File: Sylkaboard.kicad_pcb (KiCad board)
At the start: 2 copper layers, 149.6 x 125.6 mm, 117 parts, among them J1 Conn_01x04_Pin, J2 USB_C_Receptacle_USB2.0_16P, U1 RP2040-ZERO

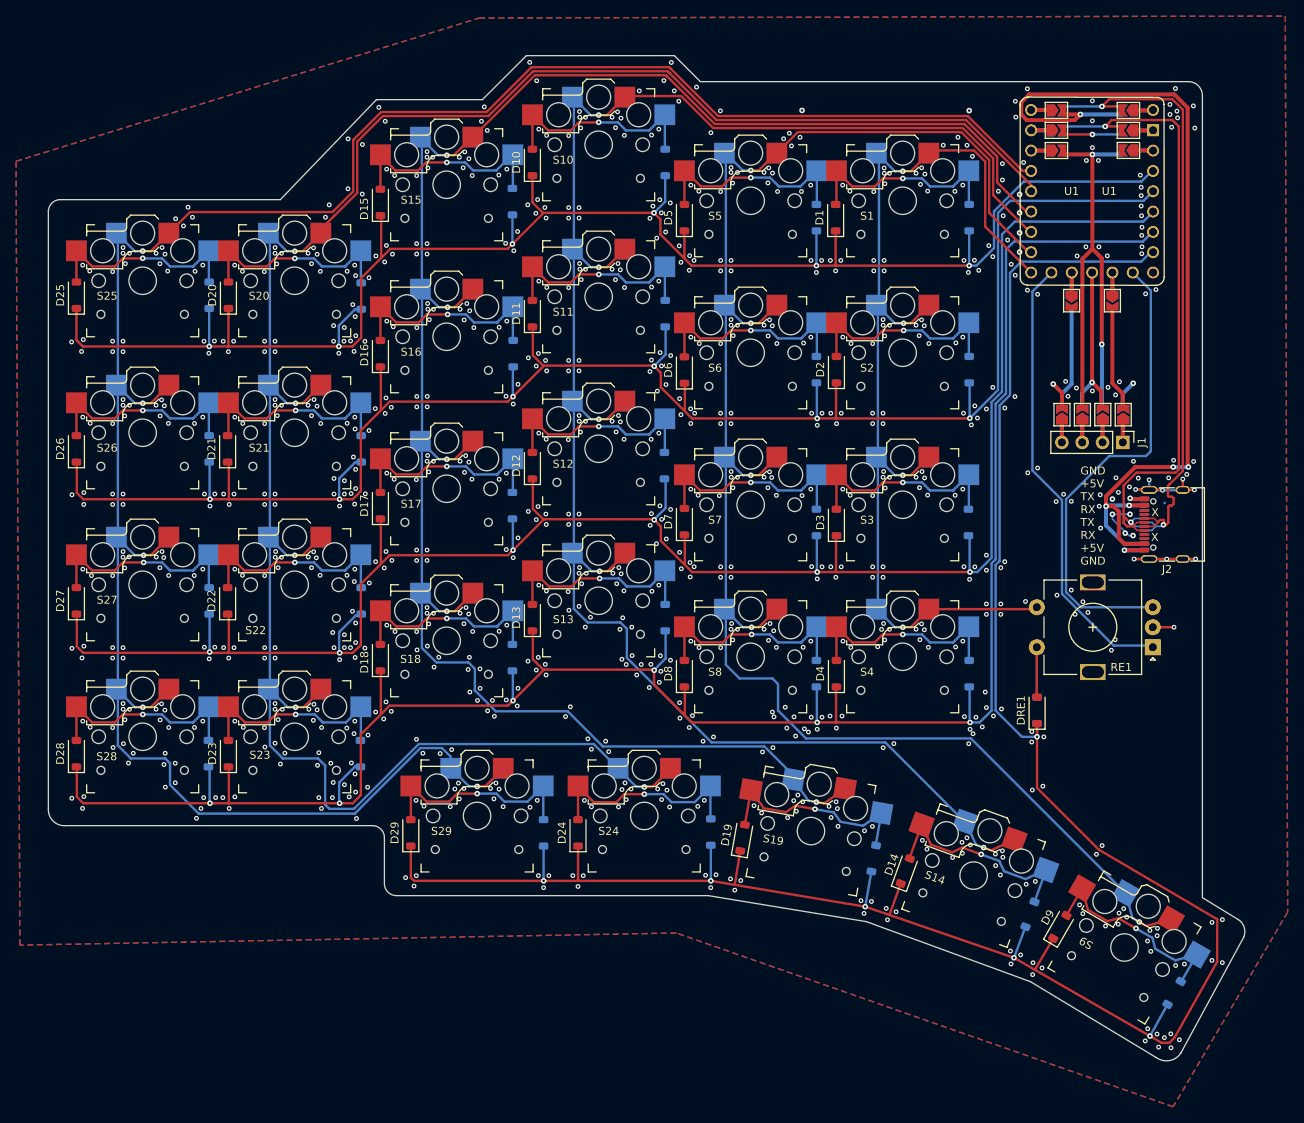
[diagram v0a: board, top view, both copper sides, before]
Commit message: Silkscreen and references modifications
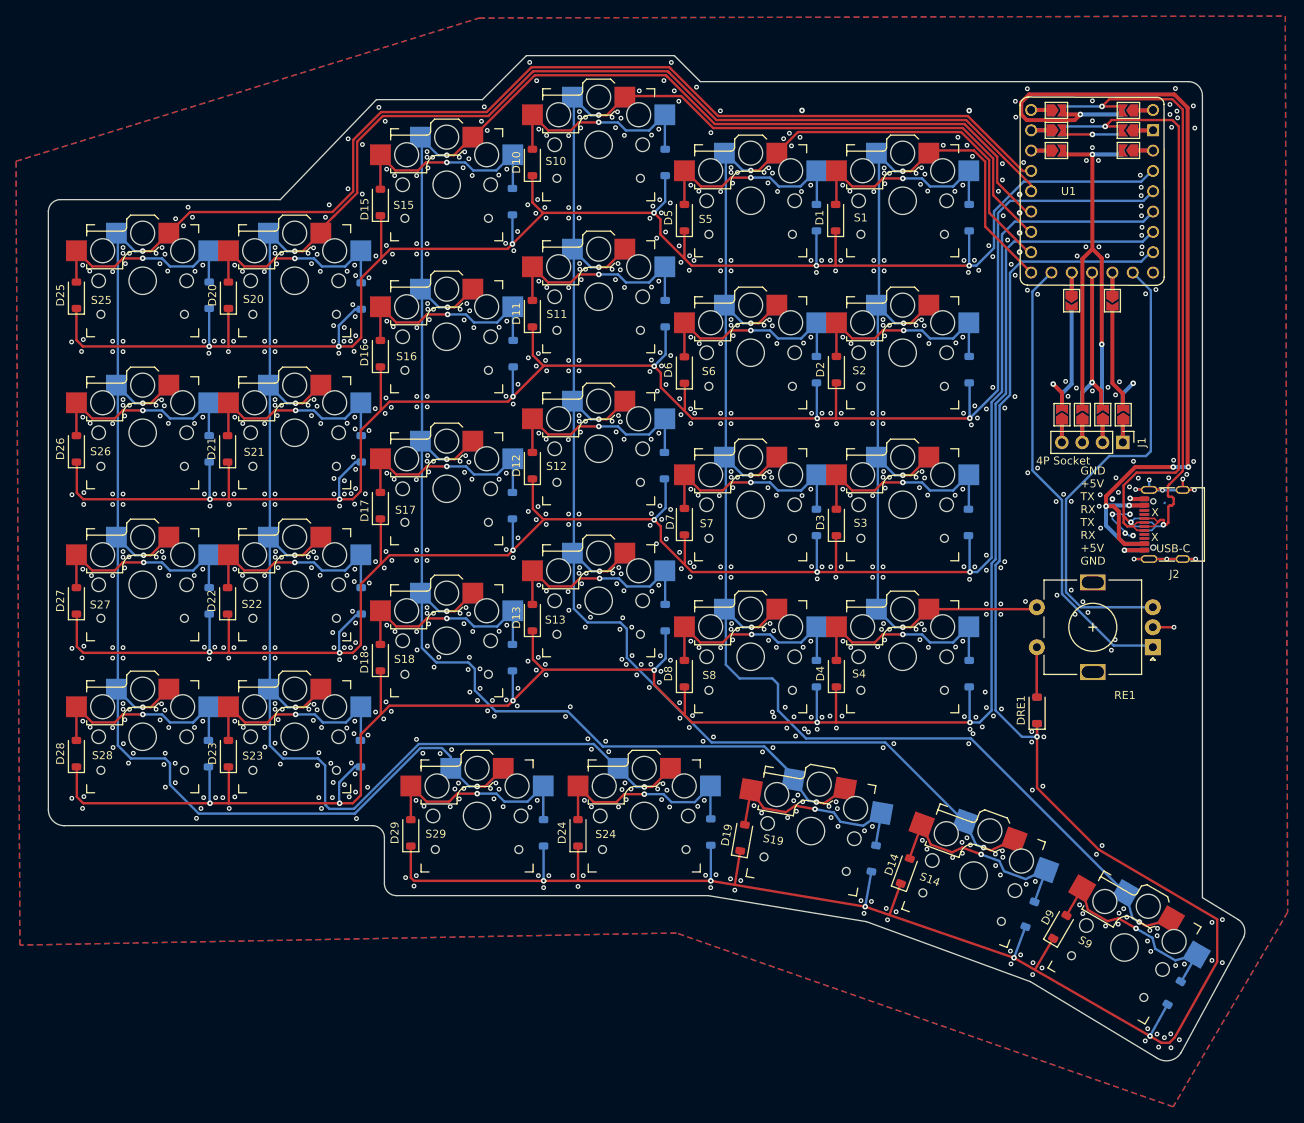
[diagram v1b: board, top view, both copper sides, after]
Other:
- board text added: "4P Socket"
- board text added: "USB-C"
- board text removed: "Conn_01x04_DISP1"

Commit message: change switch footprint to a correct dimension holes
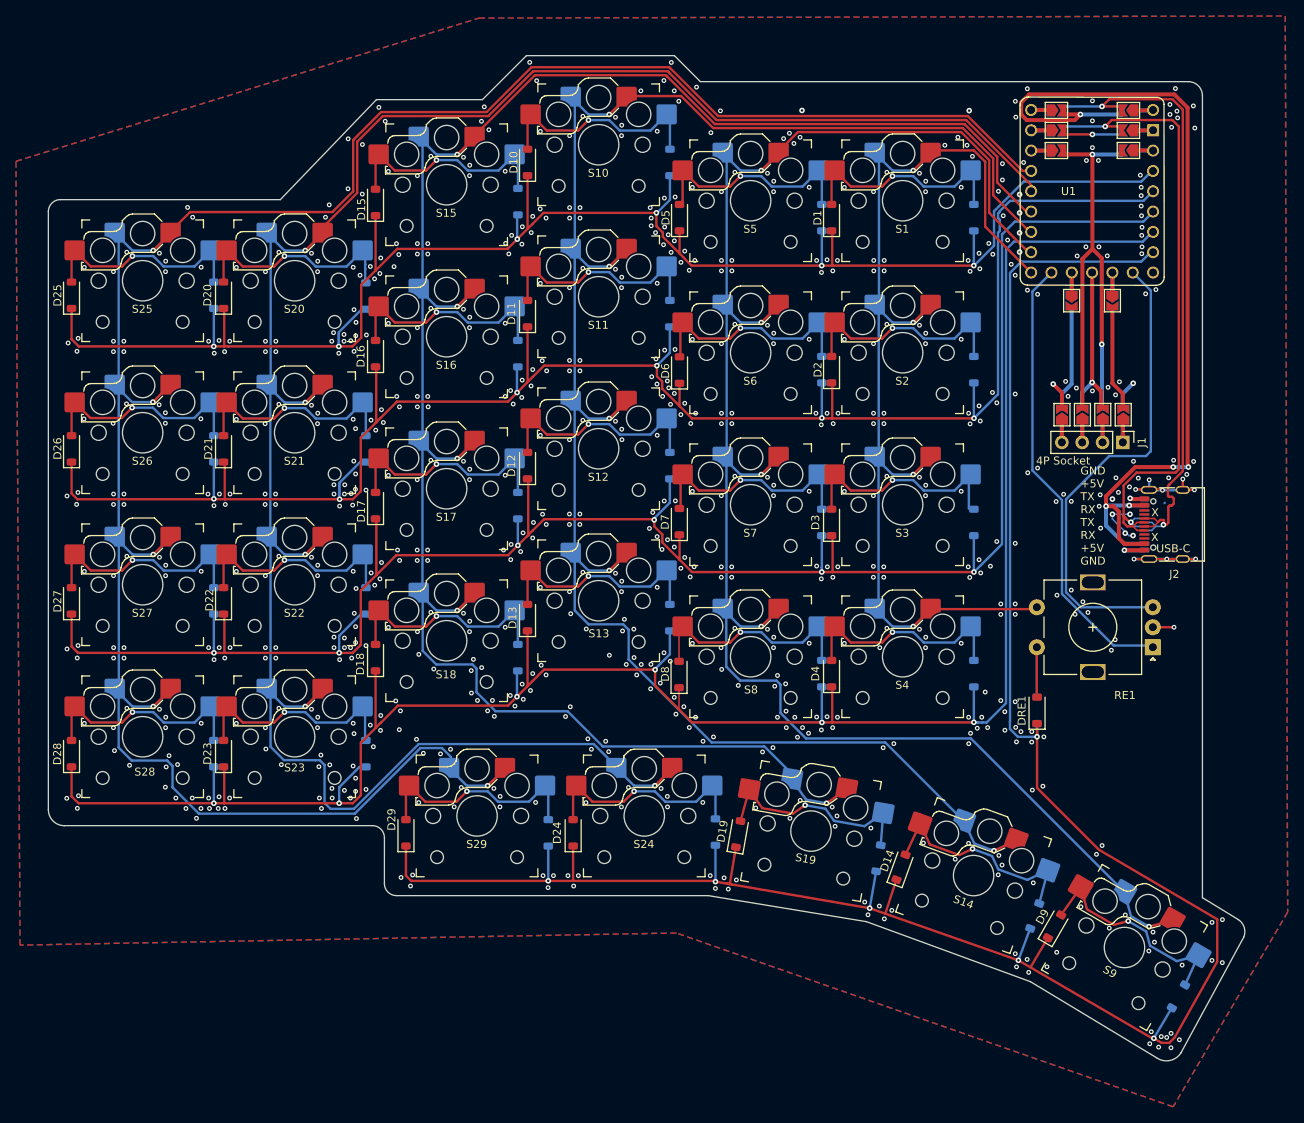
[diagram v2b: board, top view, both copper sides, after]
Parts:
- S1, S10, S11, S12, S13, S14, S15, S16, S17, S18, S19, S2, S20, S21, S22, S23, S24, S25, S26, S27, S28, S29, S3, S4, S5, S6, S7, S8, S9: footprint Footprints:Kailh_socket_PG1350_reversible -> Footprints:Kail_Hotswap_Reversible_V1V2
- moved D14 0.72 mm to (215.6, 199.7)
- moved D19 0.71 mm to (195.2, 195.6)
- moved D115 0.69 mm to (167.7, 116.5)
- moved D109 0.68 mm to (250.2, 215.8)
- moved D103 0.68 mm to (224.7, 156.6)
- moved D105 0.68 mm to (205.7, 118.5)
- moved D106 0.68 mm to (205.7, 137.5)
- moved D107 0.68 mm to (205.7, 156.6)
- moved D108 0.68 mm to (205.7, 175.5)
- moved D112 0.68 mm to (186.7, 149.5)
- moved D117 0.68 mm to (167.7, 154.5)
- moved D118 0.68 mm to (167.7, 173.5)
- moved D123 0.68 mm to (148.7, 185.5)
- moved D128 0.68 mm to (129.7, 185.5)
- moved D8 0.68 mm to (187.8, 175.6)
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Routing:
- net /row2: track 229.8 -> 236.8 mm
- net /row3: track 246.5 -> 252.1 mm
- net /row4: track 263.1 -> 267.4 mm
- net /row1: track 212.8 -> 216.9 mm
- net /col1: track 282.2 -> 285.5 mm
- net /col3: track 239.5 -> 242.4 mm
- net /col5: track 210.9 -> 213.7 mm
- net /col4: track 225.6 -> 228.1 mm
- net /col2: track 266.4 -> 268.8 mm
- net /col6: track 125.9 -> 128.0 mm
- net /SD6: track 27.4 -> 29.2 mm
- net /SD8: track 27.3 -> 28.7 mm
- net /SD21: track 27.0 -> 28.4 mm
- net /SD9: track 26.7 -> 28.1 mm
- net /SD15: track 27.4 -> 28.7 mm
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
